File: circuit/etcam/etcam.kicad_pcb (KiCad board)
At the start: 2 copper layers, 100 x 50 mm, 86 parts, among them J1 SWD_connector, J2 USB_connector, J3 ESC_signal_connector, J4 ESC_GND_connector, J5 MCU_PWR_SRC_selector, J6 jumper_park, SW1 reset_SW, U1 FT232RL, U2 Si8640BB-B-IS1, U3 Si8640BB-B-IS1, U4 Si8640BB-B-IS1, U5 Si8640BB-B-IS1, U6 74HC251, U7 STM32F303xD/E-LQFP64, U8 LM1117-3.3, U9 ADuM5020, Y1 8MHz

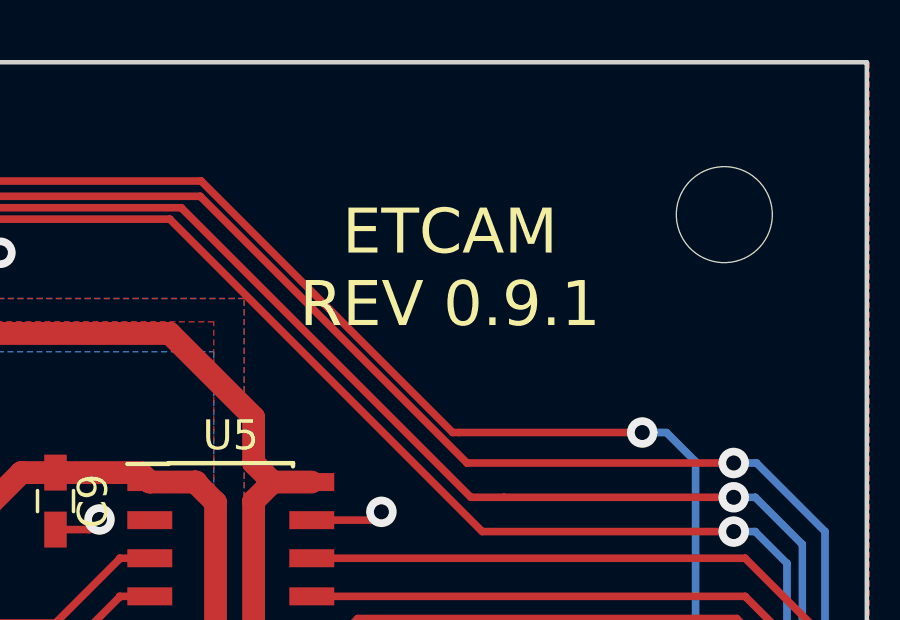
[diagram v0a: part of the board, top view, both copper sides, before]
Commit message: fixed "telementry" to "telemetry" in ETCAM
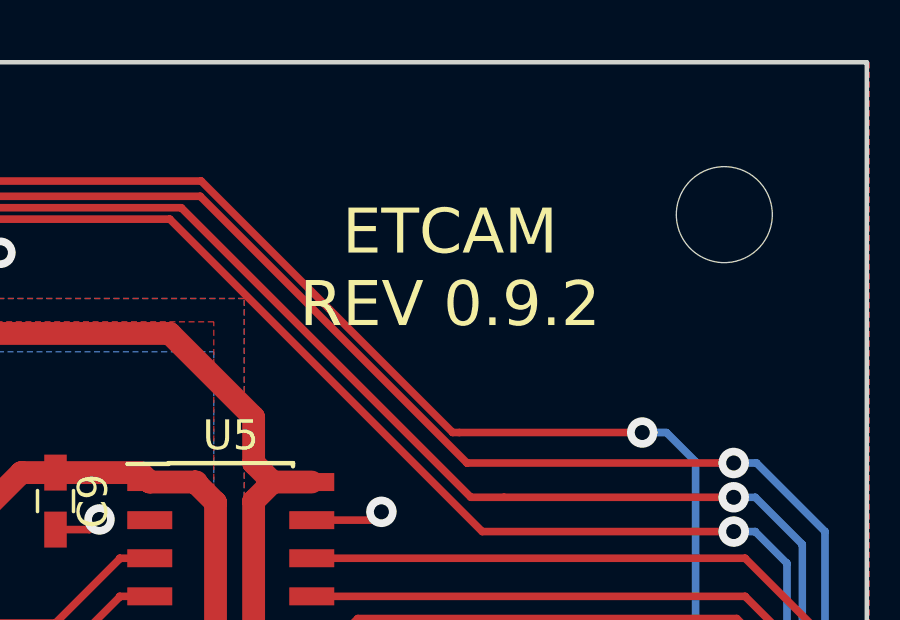
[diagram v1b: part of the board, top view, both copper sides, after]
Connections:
- net /ISOLATED_TELEMENTRY1 renamed /ISOLATED_TELEMETRY1
- net /ISOLATED_TELEMENTRY2 renamed /ISOLATED_TELEMETRY2
- net /ISOLATED_TELEMENTRY3 renamed /ISOLATED_TELEMETRY3
- net /ISOLATED_TELEMENTRY4 renamed /ISOLATED_TELEMETRY4
- net /ISOLATED_TELEMENTRY5 renamed /ISOLATED_TELEMETRY5
- net /ISOLATED_TELEMENTRY6 renamed /ISOLATED_TELEMETRY6
- net /ISOLATED_TELEMENTRY7 renamed /ISOLATED_TELEMETRY7
- net /ISOLATED_TELEMENTRY8 renamed /ISOLATED_TELEMETRY8
- net /controller/TELEMENTRY_SEL0 renamed /controller/TELEMETRY_SEL0
- net /controller/TELEMENTRY_SEL1 renamed /controller/TELEMETRY_SEL1
- net /controller/TELEMENTRY_SEL2 renamed /controller/TELEMETRY_SEL2
- net /isolation_barrier/TELEMENTRY1 renamed /isolation_barrier/TELEMETRY1
- net /isolation_barrier/TELEMENTRY2 renamed /isolation_barrier/TELEMETRY2
- net /isolation_barrier/TELEMENTRY3 renamed /isolation_barrier/TELEMETRY3
- net /isolation_barrier/TELEMENTRY4 renamed /isolation_barrier/TELEMETRY4
- net /isolation_barrier/TELEMENTRY5 renamed /isolation_barrier/TELEMETRY5
- net /isolation_barrier/TELEMENTRY6 renamed /isolation_barrier/TELEMETRY6
- net /isolation_barrier/TELEMENTRY7 renamed /isolation_barrier/TELEMETRY7
- net /isolation_barrier/TELEMENTRY8 renamed /isolation_barrier/TELEMETRY8
- net /telementry_selector/SELECTED_TELEMENTRY renamed /telementry_selector/SELECTED_TELEMETRY
- J2 pad 4: (no net) -> Net-(J2-Pad4)
- J6 pad 1: (no net) -> Net-(J6-Pad1)
- J6 pad 2: (no net) -> Net-(J6-Pad2)
- U1 pad 10: (no net) -> Net-(U1-Pad10)
- U1 pad 11: (no net) -> Net-(U1-Pad11)
- U1 pad 12: (no net) -> Net-(U1-Pad12)
- U1 pad 13: (no net) -> Net-(U1-Pad13)
- U1 pad 14: (no net) -> Net-(U1-Pad14)
- U1 pad 2: (no net) -> Net-(U1-Pad2)
- U1 pad 24: (no net) -> Net-(U1-Pad24)
- U1 pad 27: (no net) -> Net-(U1-Pad27)
- U1 pad 28: (no net) -> Net-(U1-Pad28)
- U1 pad 3: (no net) -> Net-(U1-Pad3)
- U1 pad 6: (no net) -> Net-(U1-Pad6)
- U1 pad 8: (no net) -> Net-(U1-Pad8)
- U1 pad 9: (no net) -> Net-(U1-Pad9)
- U2 pad 7: (no net) -> Net-(U2-Pad7)
- U3 pad 7: (no net) -> Net-(U3-Pad7)
- U4 pad 7: (no net) -> Net-(U4-Pad7)
- U5 pad 7: (no net) -> Net-(U5-Pad7)
- U6 pad 6: (no net) -> Net-(U6-Pad6)
- U7 pad 10: (no net) -> Net-(U7-Pad10)
- U7 pad 11: (no net) -> Net-(U7-Pad11)
- U7 pad 14: (no net) -> Net-(U7-Pad14)
- U7 pad 15: (no net) -> Net-(U7-Pad15)
- U7 pad 16: (no net) -> Net-(U7-Pad16)
- U7 pad 2: (no net) -> Net-(U7-Pad2)
- U7 pad 23: (no net) -> Net-(U7-Pad23)
- U7 pad 24: (no net) -> Net-(U7-Pad24)
- U7 pad 25: (no net) -> Net-(U7-Pad25)
- U7 pad 26: (no net) -> Net-(U7-Pad26)
- U7 pad 27: (no net) -> Net-(U7-Pad27)
- U7 pad 28: (no net) -> Net-(U7-Pad28)
- U7 pad 29: (no net) -> Net-(U7-Pad29)
- U7 pad 3: (no net) -> Net-(U7-Pad3)
- U7 pad 30: (no net) -> Net-(U7-Pad30)
- U7 pad 33: (no net) -> Net-(U7-Pad33)
- U7 pad 34: (no net) -> Net-(U7-Pad34)
- U7 pad 35: (no net) -> Net-(U7-Pad35)
- U7 pad 36: (no net) -> Net-(U7-Pad36)
- U7 pad 4: (no net) -> Net-(U7-Pad4)
- U7 pad 41: (no net) -> Net-(U7-Pad41)
- U7 pad 50: (no net) -> Net-(U7-Pad50)
- U7 pad 51: (no net) -> Net-(U7-Pad51)
- U7 pad 52: (no net) -> Net-(U7-Pad52)
- U7 pad 53: (no net) -> Net-(U7-Pad53)
- U7 pad 54: (no net) -> Net-(U7-Pad54)
- U7 pad 56: (no net) -> Net-(U7-Pad56)
- U7 pad 57: (no net) -> Net-(U7-Pad57)
- U7 pad 8: (no net) -> Net-(U7-Pad8)
- U7 pad 9: (no net) -> Net-(U7-Pad9)
- U9 pad 1: (no net) -> Net-(U9-Pad1)
- U9 pad 10: (no net) -> Net-(U9-Pad10)
- U9 pad 16: (no net) -> Net-(U9-Pad16)
- U9 pad 7: (no net) -> Net-(U9-Pad7)
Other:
- board text added: "ETCAM REV 0.9.2"
- board text removed: "ETCAM REV 0.9.1"

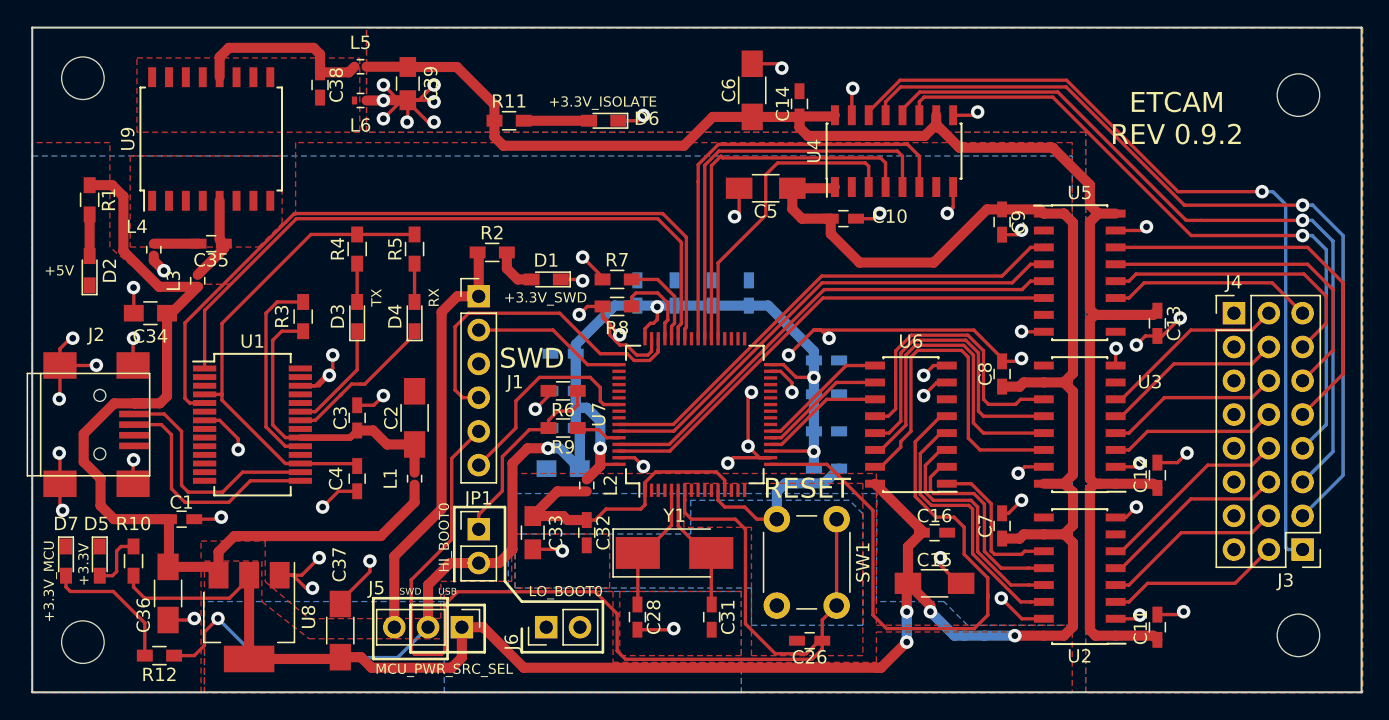
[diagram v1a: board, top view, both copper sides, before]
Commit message: fixed +3.3V_ISOLATOR cut GND_PWR plane in ETCAM PCB
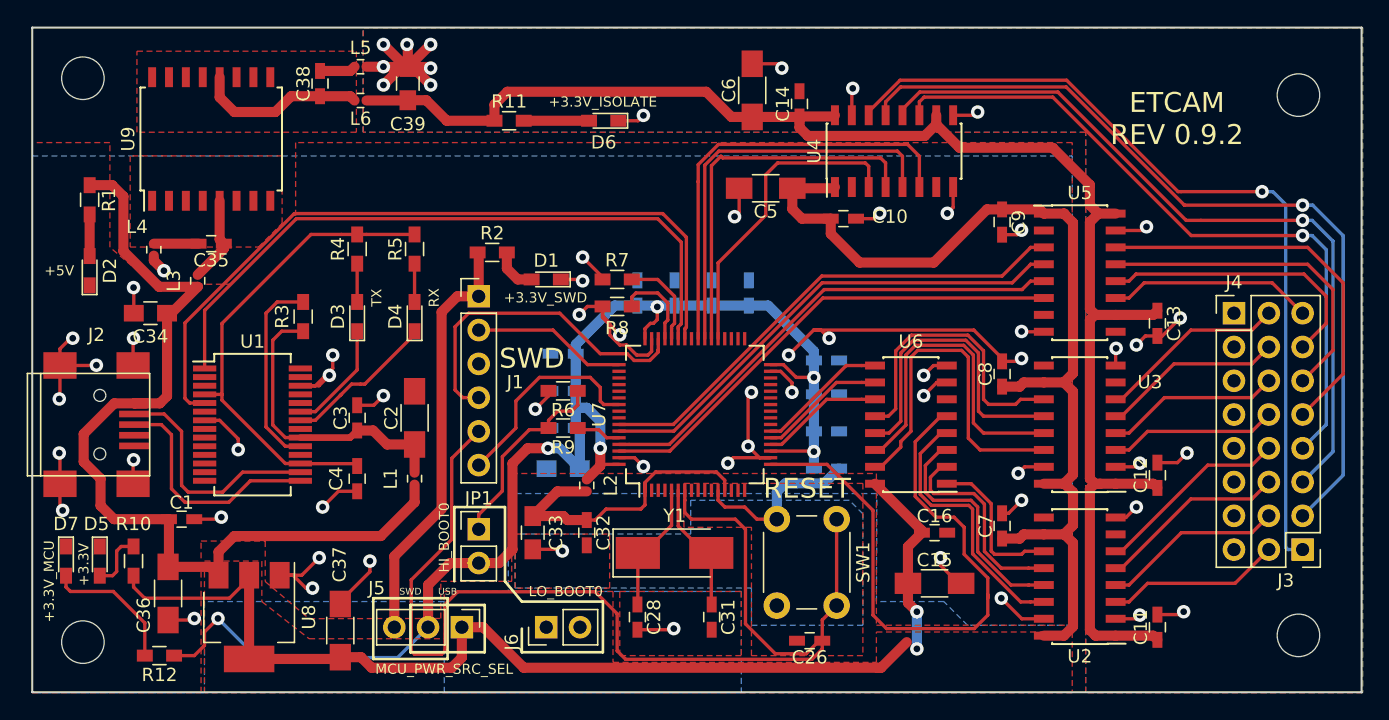
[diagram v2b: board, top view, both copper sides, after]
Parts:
- moved L5 2.54 mm to (117.6, 72.6)
- moved L6 2.54 mm to (117.6, 70.1)
- moved C38 0.10 mm to (114.6, 71.4), turned to 90 degrees
- turned C39 to 90 degrees
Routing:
- net /+3.3V_USB: track 174.1 -> 162.5 mm, vias 4 -> 2
- net Net-(C38-Pad2): track 0.00 -> 2.73 mm
- net /+3.3V_ISOLATOR: track 116.9 -> 115.2 mm
- net Net-(C38-Pad1): track 13.7 -> 12.7 mm

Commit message: rearranged mounting holes of ETCAM PCB
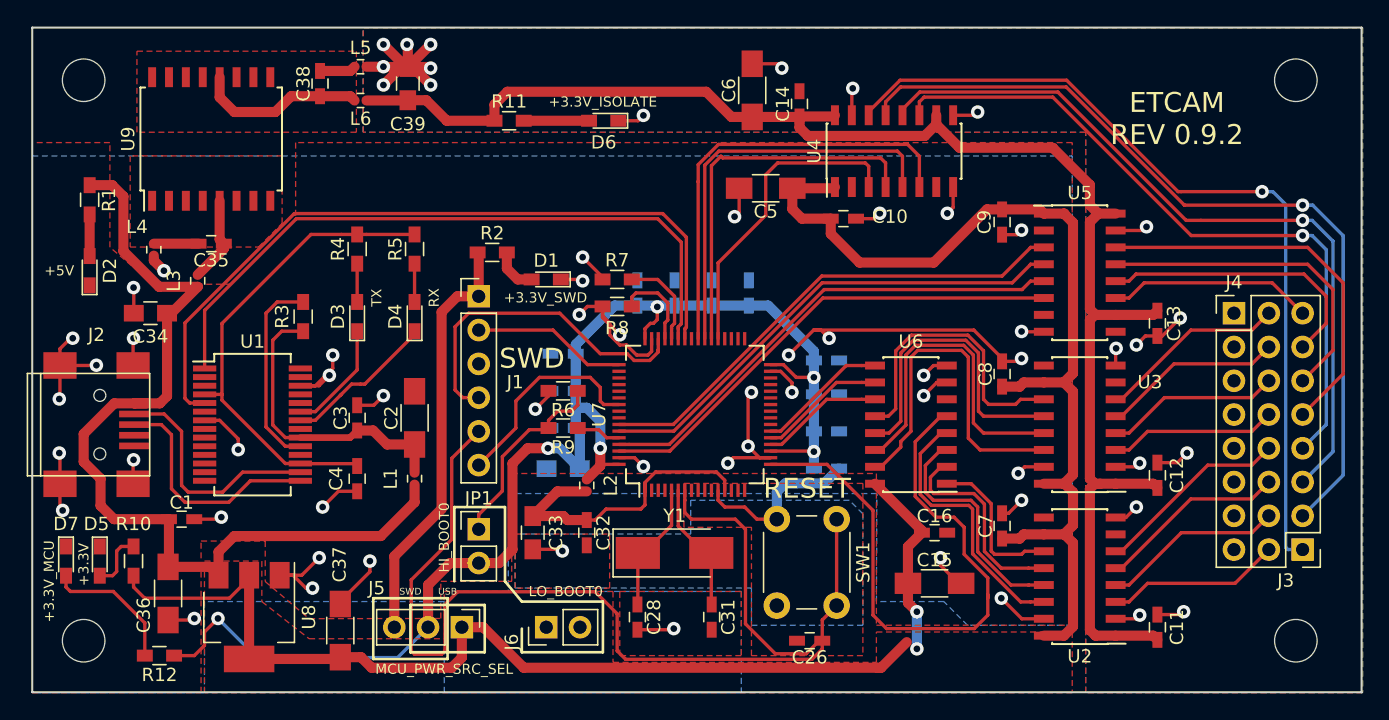
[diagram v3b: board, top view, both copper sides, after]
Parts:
- moved C20 10.0 mm to (152.7, 92.2), turned to 0 degrees
- moved C22 10.0 mm to (144.0, 87.1), turned to 90 degrees
- moved C23 9.55 mm to (141.2, 87.1), turned to 90 degrees
- moved C25 9.55 mm to (132.8, 91.7), turned to 180 degrees
- moved ? 1.14 mm to (188.0, 71.1)
- moved ? 0.45 mm to (188.0, 113.3)
- moved ? 0.16 mm to (96.8, 71.1)
- moved ? 0.12 mm to (96.8, 113.3)
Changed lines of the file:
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@@
   )
   (setup
-    (last_trace_width 0.762)
+    (last_trace_width 0.254)
     (user_trace_width 0.508)
     (user_trace_width 0.762)
@@
     (mod_text_size 1 1)
     (mod_text_width 0.15)
-    (pad_size 1.524 1.524)
-    (pad_drill 0.762)
+    (pad_size 3.2 3.2)
+    (pad_drill 3.2)
     (pad_to_mask_clearance 0.2)
     (aux_axis_origin 92.906 67.16)
     (grid_origin 92.906 67.16)
-    (visible_elements 7FFFEFFF)
+    (visible_elements 7FFFFFFF)
     (pcbplotparams
       (layerselection 0x00030_80000001)
@@
     (tags "capacitor 0603")
     (attr smd)
-    (fp_text reference C18 (at 0 1.25) (layer B.SilkS)
+    (fp_text reference C18 (at 0 -1.42) (layer B.SilkS)
       (effects (font (size 1 1) (thickness 0.15)) (justify mirror))
     )
@@
     (tags "capacitor 0603")
     (attr smd)
-    (fp_text reference C9 (at 0 -1.25 270) (layer F.SilkS)
+    (fp_text reference C9 (at 0 1.328 270) (layer F.SilkS)
       (effects (font (size 1 1) (thickness 0.15)))
     )
@@
     (tags "capacitor 0603")
     (attr smd)
-    (fp_text reference C11 (at 0 -1.25 90) (layer F.SilkS)
+    (fp_text reference C11 (at 0 1.466 90) (layer F.SilkS)
       (effects (font (size 1 1) (thickness 0.15)))
     )
@@
     (tags "capacitor 0603")
     (attr smd)
-    (fp_text reference C12 (at 0 -1.25 90) (layer F.SilkS)
+    (fp_text reference C12 (at 0 1.466 90) (layer F.SilkS)
       (effects (font (size 1 1) (thickness 0.15)))
     )
@@
     (tags "capacitor 0603")
     (attr smd)
-    (fp_text reference C17 (at 0 1.25) (layer B.SilkS)
+    (fp_text reference C17 (at 0 -1.42) (layer B.SilkS)
       (effects (font (size 1 1) (thickness 0.15)) (justify mirror))
     )
@@
     (tags "capacitor 0603")
     (attr smd)
-    (fp_text reference C19 (at 0 1.25) (layer B.SilkS)
+    (fp_text reference C19 (at 0 -1.166) (layer B.SilkS)
       (effects (font (size 1 1) (thickness 0.15)) (justify mirror))
     )
@@
   )
   (module Capacitors_SMD:C_0603_HandSoldering (layer B.Cu)
-    (at 144.018 87.122 90)
+    (at 152.654 92.202)
     (descr "Capacitor SMD 0603, hand soldering")
     (tags "capacitor 0603")
     (attr smd)
-    (fp_text reference C20 (at 0 1.25 90) (layer B.SilkS)
+    (fp_text reference C20 (at 0 -1.42) (layer B.SilkS)
       (effects (font (size 1 1) (thickness 0.15)) (justify mirror))
     )
-    (fp_text value 0.1uF (at 0 -1.5 90) (layer B.Fab)
+    (fp_text value 0.1uF (at 0 -1.5) (layer B.Fab)
       (effects (font (size 1 1) (thickness 0.15)) (justify mirror))
     )
-    (fp_text user %R (at 0 1.25 90) (layer B.Fab)
+    (fp_text user %R (at 0 1.25) (layer B.Fab)
       (effects (font (size 1 1) (thickness 0.15)) (justify mirror))
     )
@@
     (fp_line (start 1.8 -0.65) (end 1.8 0.65) (layer B.CrtYd) (width 0.05))
     (fp_line (start 1.8 -0.65) (end -1.8 -0.65) (layer B.CrtYd) (width 0.05))
-    (pad 1 smd rect (at -0.95 0 90) (size 1.2 0.75) (layers B.Cu B.Paste B.Mask)
+    (pad 1 smd rect (at -0.95 0) (size 1.2 0.75) (layers B.Cu B.Paste B.Mask)
       (net 8 /controller/+3.3V_CONTROLLER))
-    (pad 2 smd rect (at 0.95 0 90) (size 1.2 0.75) (layers B.Cu B.Paste B.Mask)
+    (pad 2 smd rect (at 0.95 0) (size 1.2 0.75) (layers B.Cu B.Paste B.Mask)
       (net 2 GND))
     (model Capacitors_SMD.3dshapes/C_0603.wrl
@@
   )
   (module Capacitors_SMD:C_0603_HandSoldering (layer B.Cu)
-    (at 152.654 92.202)
+    (at 144.018 87.122 90)
     (descr "Capacitor SMD 0603, hand soldering")
     (tags "capacitor 0603")
     (attr smd)
-    (fp_text reference C22 (at 0 1.25) (layer B.SilkS)
+    (fp_text reference C22 (at 0 1.25 90) (layer B.SilkS)
       (effects (font (size 1 1) (thickness 0.15)) (justify mirror))
     )
-    (fp_text value 0.1uF (at 0 -1.5) (layer B.Fab)
+    (fp_text value 0.1uF (at 0 -1.5 90) (layer B.Fab)
       (effects (font (size 1 1) (thickness 0.15)) (justify mirror))
     )
-    (fp_text user %R (at 0 1.25) (layer B.Fab)
+    (fp_text user %R (at 0 1.25 90) (layer B.Fab)
       (effects (font (size 1 1) (thickness 0.15)) (justify mirror))
     )
@@
     (fp_line (start 1.8 -0.65) (end 1.8 0.65) (layer B.CrtYd) (width 0.05))
     (fp_line (start 1.8 -0.65) (end -1.8 -0.65) (layer B.CrtYd) (width 0.05))
-    (pad 1 smd rect (at -0.95 0) (size 1.2 0.75) (layers B.Cu B.Paste B.Mask)
+    (pad 1 smd rect (at -0.95 0 90) (size 1.2 0.75) (layers B.Cu B.Paste B.Mask)
       (net 8 /controller/+3.3V_CONTROLLER))
-    (pad 2 smd rect (at 0.95 0) (size 1.2 0.75) (layers B.Cu B.Paste B.Mask)
+    (pad 2 smd rect (at 0.95 0 90) (size 1.2 0.75) (layers B.Cu B.Paste B.Mask)
       (net 2 GND))
     (model Capacitors_SMD.3dshapes/C_0603.wrl
@@
   )
   (module Capacitors_SMD:C_0603_HandSoldering (layer B.Cu)
-    (at 132.842 91.694 180)
+    (at 141.224 87.122 90)
     (descr "Capacitor SMD 0603, hand soldering")
     (tags "capacitor 0603")
     (attr smd)
-    (fp_text reference C23 (at 0 1.25 180) (layer B.SilkS)
+    (fp_text reference C23 (at 0 1.25 90) (layer B.SilkS)
       (effects (font (size 1 1) (thickness 0.15)) (justify mirror))
     )
-    (fp_text value 0.1uF (at 0 -1.5 180) (layer B.Fab)
+    (fp_text value 0.1uF (at 0 -1.5 90) (layer B.Fab)
       (effects (font (size 1 1) (thickness 0.15)) (justify mirror))
     )
-    (fp_text user %R (at 0 1.25 180) (layer B.Fab)
+    (fp_text user %R (at 0 1.25 90) (layer B.Fab)
       (effects (font (size 1 1) (thickness 0.15)) (justify mirror))
     )
@@
     (fp_line (start 1.8 -0.65) (end 1.8 0.65) (layer B.CrtYd) (width 0.05))
     (fp_line (start 1.8 -0.65) (end -1.8 -0.65) (layer B.CrtYd) (width 0.05))
-    (pad 1 smd rect (at -0.95 0 180) (size 1.2 0.75) (layers B.Cu B.Paste B.Mask)
+    (pad 1 smd rect (at -0.95 0 90) (size 1.2 0.75) (layers B.Cu B.Paste B.Mask)
       (net 8 /controller/+3.3V_CONTROLLER))
-    (pad 2 smd rect (at 0.95 0 180) (size 1.2 0.75) (layers B.Cu B.Paste B.Mask)
+    (pad 2 smd rect (at 0.95 0 90) (size 1.2 0.75) (layers B.Cu B.Paste B.Mask)
       (net 2 GND))
     (model Capacitors_SMD.3dshapes/C_0603.wrl
@@
   )
   (module Capacitors_SMD:C_0603_HandSoldering (layer B.Cu)
-    (at 141.224 87.122 90)
+    (at 132.842 91.694 180)
     (descr "Capacitor SMD 0603, hand soldering")
     (tags "capacitor 0603")
     (attr smd)
-    (fp_text reference C25 (at 0 1.25 90) (layer B.SilkS)
+    (fp_text reference C25 (at 0 1.25 180) (layer B.SilkS)
       (effects (font (size 1 1) (thickness 0.15)) (justify mirror))
     )
-    (fp_text value 0.1uF (at 0 -1.5 90) (layer B.Fab)
+    (fp_text value 0.1uF (at 0 -1.5 180) (layer B.Fab)
       (effects (font (size 1 1) (thickness 0.15)) (justify mirror))
     )
-    (fp_text user %R (at 0 1.25 90) (layer B.Fab)
+    (fp_text user %R (at 0 1.25 180) (layer B.Fab)
       (effects (font (size 1 1) (thickness 0.15)) (justify mirror))
     )
@@
     (fp_line (start 1.8 -0.65) (end 1.8 0.65) (layer B.CrtYd) (width 0.05))
     (fp_line (start 1.8 -0.65) (end -1.8 -0.65) (layer B.CrtYd) (width 0.05))
-    (pad 1 smd rect (at -0.95 0 90) (size 1.2 0.75) (layers B.Cu B.Paste B.Mask)
+    (pad 1 smd rect (at -0.95 0 180) (size 1.2 0.75) (layers B.Cu B.Paste B.Mask)
       (net 8 /controller/+3.3V_CONTROLLER))
-    (pad 2 smd rect (at 0.95 0 90) (size 1.2 0.75) (layers B.Cu B.Paste B.Mask)
+    (pad 2 smd rect (at 0.95 0 180) (size 1.2 0.75) (layers B.Cu B.Paste B.Mask)
       (net 2 GND))
     (model Capacitors_SMD.3dshapes/C_0603.wrl
@@
   )
   (module Mounting_Holes:MountingHole_3.2mm_M3 (layer F.Cu)
-    (at 188.156 72.24)
+    (at 187.96 71.12)
     (descr "Mounting Hole 3.2mm, no annular, M3")
     (tags "mounting hole 3.2mm no annular m3")
@@
   )
   (module Mounting_Holes:MountingHole_3.2mm_M3 (layer F.Cu)
-    (at 188.156 112.88)
+    (at 187.96 113.284)
     (descr "Mounting Hole 3.2mm, no annular, M3")
     (tags "mounting hole 3.2mm no annular m3")
@@
   )
   (module Mounting_Holes:MountingHole_3.2mm_M3 (layer F.Cu)
-    (at 96.716 70.97)
+    (at 96.774 71.12)
     (descr "Mounting Hole 3.2mm, no annular, M3")
     (tags "mounting hole 3.2mm no annular m3")
@@
   )
   (module Mounting_Holes:MountingHole_3.2mm_M3 (layer F.Cu)
-    (at 96.716 113.388)
+    (at 96.774 113.284)
     (descr "Mounting Hole 3.2mm, no annular, M3")
     (tags "mounting hole 3.2mm no annular m3")
